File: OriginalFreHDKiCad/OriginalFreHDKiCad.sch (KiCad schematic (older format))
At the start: 48 parts, among them J1 CON5, J2 SDCARD, J3 CON50, J4 CON2, J5 CON5, Q1 BS170, U1 PIC18F4610, U2 GAL16V8, U3 74HCT245, U4 LP2950-3.3, U5 MAX232, U6 74HC595, U7 DS1307+, Y1 10MHz, Y2 32.768kHz

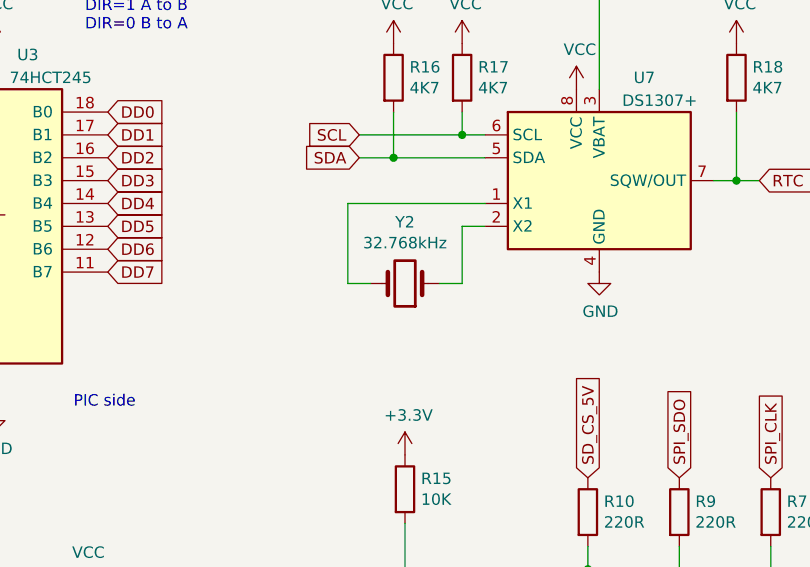
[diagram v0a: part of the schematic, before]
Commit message: WIP on matching scheamtic to imported gerbers.
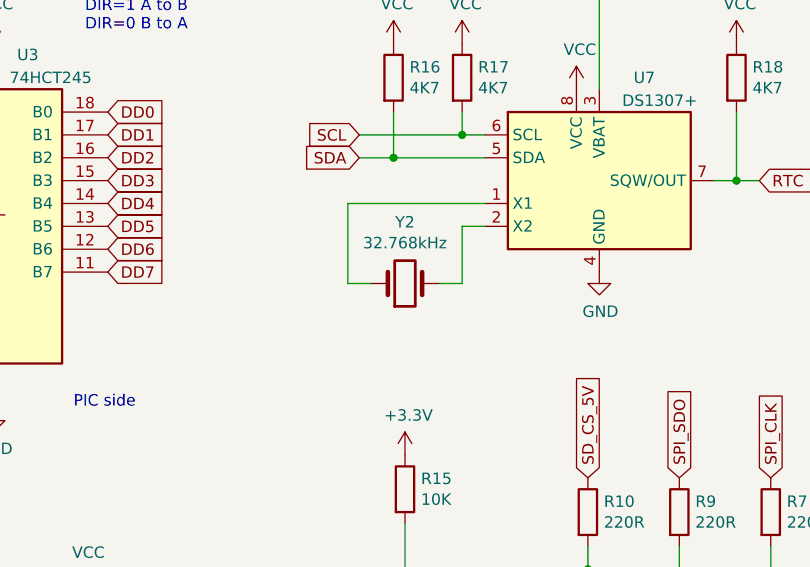
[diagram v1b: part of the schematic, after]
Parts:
- BAT1: footprint (none) -> Battery:BatteryHolder_Keystone_1060_1x2032
- C1: footprint (none) -> Fuse:Fuseholder_Blade_Mini_Keystone_3568
- C11, C12, C19, C5, C6, C7, C8: footprint (none) -> Capacitor_THT:CP_Radial_D7.5mm_P2.50mm
- C2, C3, C4, C9: footprint (none) -> Capacitor_THT:C_Disc_D8.0mm_W2.5mm_P5.00mm
- D1, D2: footprint (none) -> LED_THT:LED_D5.0mm
- J1, J5: footprint (none) -> Connector_PinHeader_2.54mm:PinHeader_1x05_P2.54mm_Vertical
- J2: footprint (none) -> Connector_Card:SD_TE_2041021
- J3: footprint (none) -> Connector_PinHeader_2.54mm:PinHeader_2x25_P2.54mm_Vertical
- J4: footprint (none) -> Connector_PinHeader_2.54mm:PinHeader_1x04_P2.54mm_Horizontal
- Q1: footprint Package_TO_SOT_THT:TO-92_Inline -> Package_TO_SOT_THT:TO-92
- R1, R10, R11, R12, R13, R14, R15, R16, R17, R18, R2, R3, R4, R5, R6, R7, R8, R9: footprint (none) -> Resistor_THT:R_Axial_DIN0207_L6.3mm_D2.5mm_P10.16mm_Horizontal
- U1: footprint (none) -> Package_DIP:DIP-40_W15.24mm
- U2, U3: footprint (none) -> Package_DIP:DIP-20_W7.62mm
- U4: footprint (none) -> Package_TO_SOT_THT:TO-92
- U5, U6: footprint (none) -> Package_DIP:DIP-16_W7.62mm
- Y1: footprint (none) -> Crystal:Crystal_HC50_Vertical
- Y2: footprint (none) -> Crystal:Crystal_C38-LF_D3.0mm_L8.0mm_Horizontal
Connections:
- net at U7.1 (X1): now also Y2.1; no longer Y2.2
- net at U7.2 (X2): now also Y2.2; no longer Y2.1

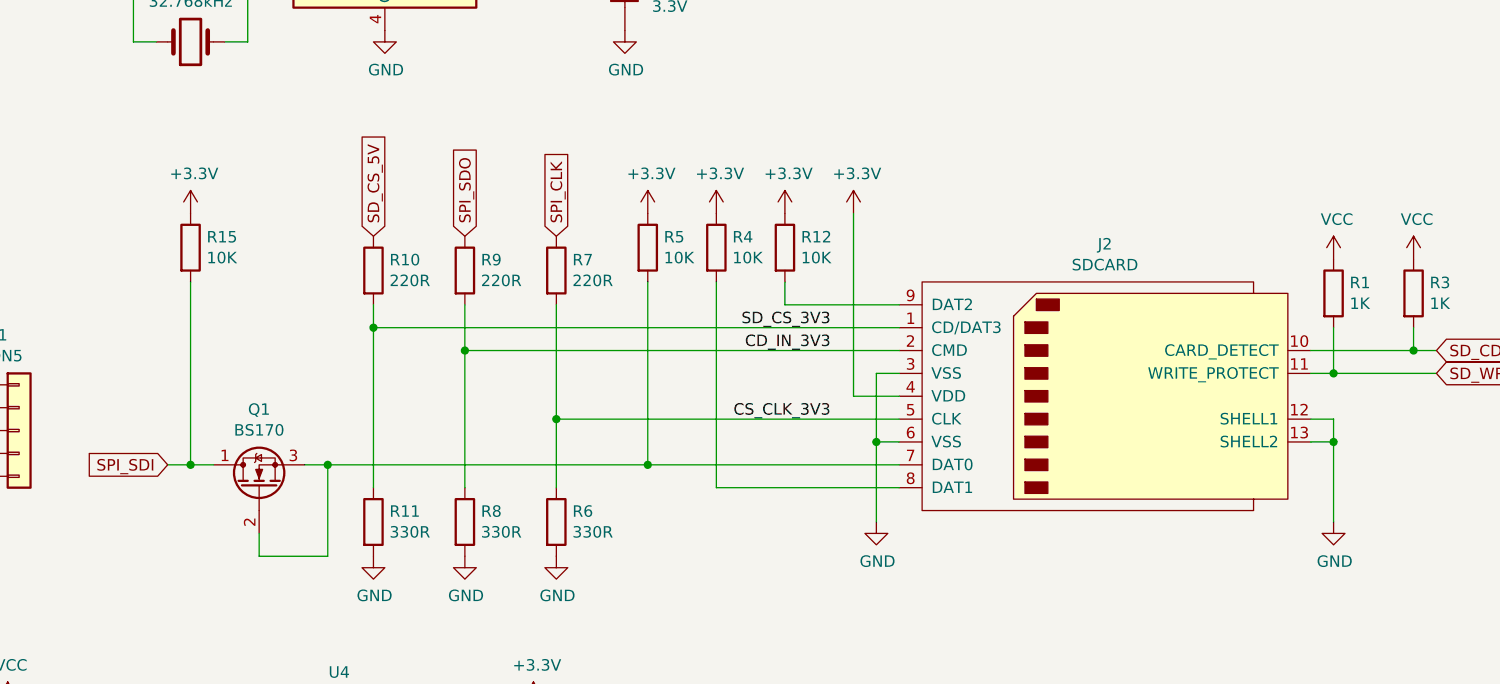
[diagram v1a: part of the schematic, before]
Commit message: Finish matching schematic to imported gerbers - the process found one small error.
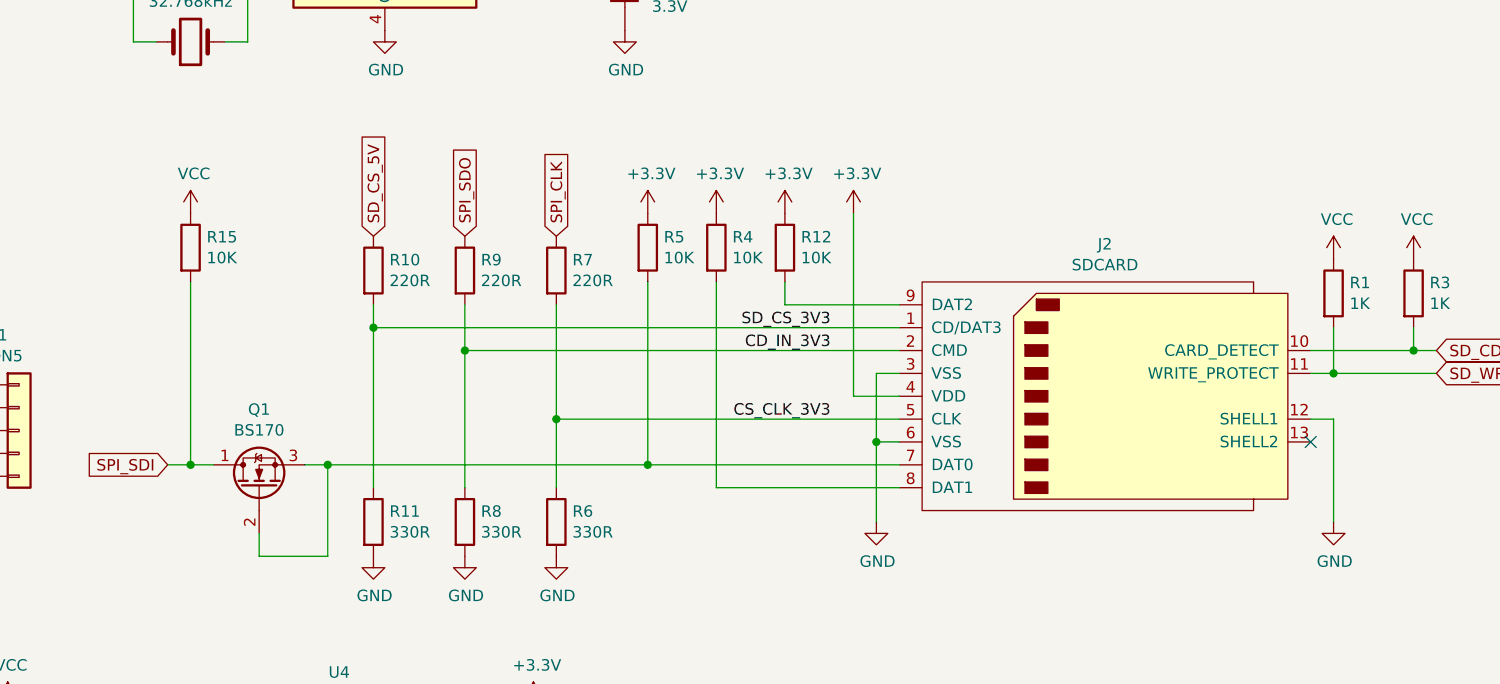
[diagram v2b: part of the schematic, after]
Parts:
- C1: footprint Fuse:Fuseholder_Blade_Mini_Keystone_3568 -> Capacitor_THT:C_Disc_D8.0mm_W2.5mm_P5.00mm
- J4: footprint Connector_PinHeader_2.54mm:PinHeader_1x04_P2.54mm_Horizontal -> Connector_PinHeader_2.54mm:PinHeader_2x01_P2.54mm_Vertical
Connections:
- net +3V3: no longer R15.1
- net GND: no longer J2.13 (SHELL2)
- net VCC: now also R15.1
- no-connect marks 5 -> 6
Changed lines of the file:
@@
 F 0 "J4" H 3718 6683 50  0000 C CNN
 F 1 "CON2" H 3718 6774 50  0000 C CNN
-F 2 "Connector_PinHeader_2.54mm:PinHeader_1x04_P2.54mm_Horizontal" H 3800 7000 50  0001 C CNN
+F 2 "Connector_PinHeader_2.54mm:PinHeader_2x01_P2.54mm_Vertical" H 3800 7000 50  0001 C CNN
 F 3 "~" H 3800 7000 50  0001 C CNN
 	1    3800 7000
@@
 F 0 "C1" H 4465 7196 50  0000 L CNN
 F 1 "0.1uF" H 4465 7105 50  0000 L CNN
-F 2 "Fuse:Fuseholder_Blade_Mini_Keystone_3568" H 4388 7000 50  0001 C CNN
+F 2 "Capacitor_THT:C_Disc_D8.0mm_W2.5mm_P5.00mm" H 4388 7000 50  0001 C CNN
 F 3 "~" H 4350 7150 50  0001 C CNN
 	1    4350 7150
@@
 Wire Wire Line
 	10050 5550 10150 5550
-Wire Wire Line
-	10150 5550 10150 5650
-Wire Wire Line
-	10050 5650 10150 5650
-Connection ~ 10150 5650
-Wire Wire Line
-	10150 5650 10150 6000
 $Comp
 L Device:R R1
@@
 Wire Wire Line
 	5150 5750 5050 5750
-$Comp
-L power:+3.3V #PWR0149
-U 1 1 60A57302
-P 5150 4650
-F 0 "#PWR0149" H 5150 4500 50  0001 C CNN
-F 1 "+3.3V" H 5165 4823 50  0000 C CNN
-F 2 "" H 5150 4650 50  0001 C CNN
-F 3 "" H 5150 4650 50  0001 C CNN
-	1    5150 4650
-	1    0    0    -1
-$EndComp
 Text GLabel 5050 5750 0    50   Input ~ 0
 SPI_SDI
@@
 $EndComp
 NoConn ~ 950  3200
+Wire Wire Line
+	10150 5550 10150 6000
+NoConn ~ 10050 5650
+$Comp
+L power:VCC #PWR?
+U 1 1 6088DA35
+P 5150 4650
+F 0 "#PWR?" H 5150 4500 50  0001 C CNN
+F 1 "VCC" H 5165 4823 50  0000 C CNN
+F 2 "" H 5150 4650 50  0001 C CNN
+F 3 "" H 5150 4650 50  0001 C CNN
+	1    5150 4650
+	1    0    0    -1
+$EndComp
 $EndSCHEMATC
